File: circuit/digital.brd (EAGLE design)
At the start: 56.2 x 50.8 mm, 31 parts, among them IC1 MCP1701-5V, IC2 MCP1700-3.3V, X1 MINI-USB-SCHIELD-32005-301

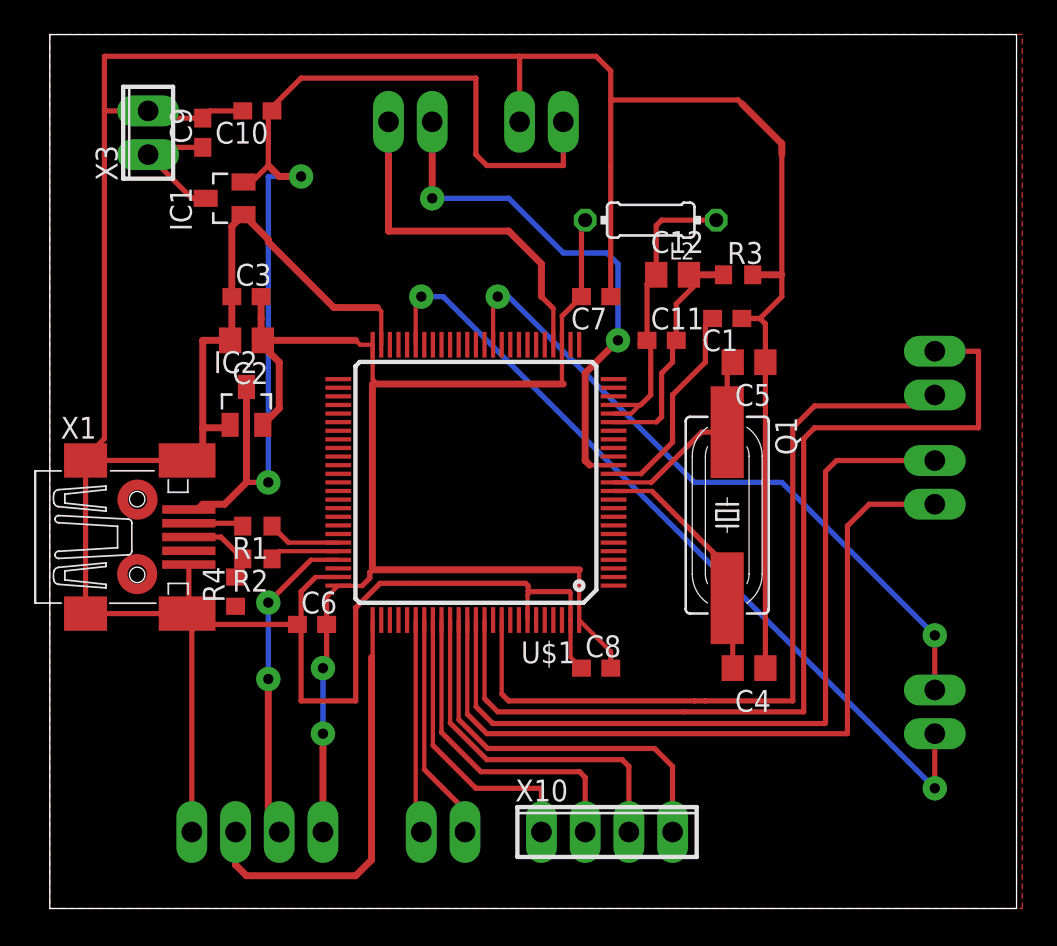
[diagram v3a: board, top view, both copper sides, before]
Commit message: - на цифровой схеме добавили разъем для Nokia 5110, коннекторы для переключения питания, объединили восточный разъем - на аналоговой схеме добавили включение 3.3 nF конденсатор, для фильтрации высокочастотных шумов ADC
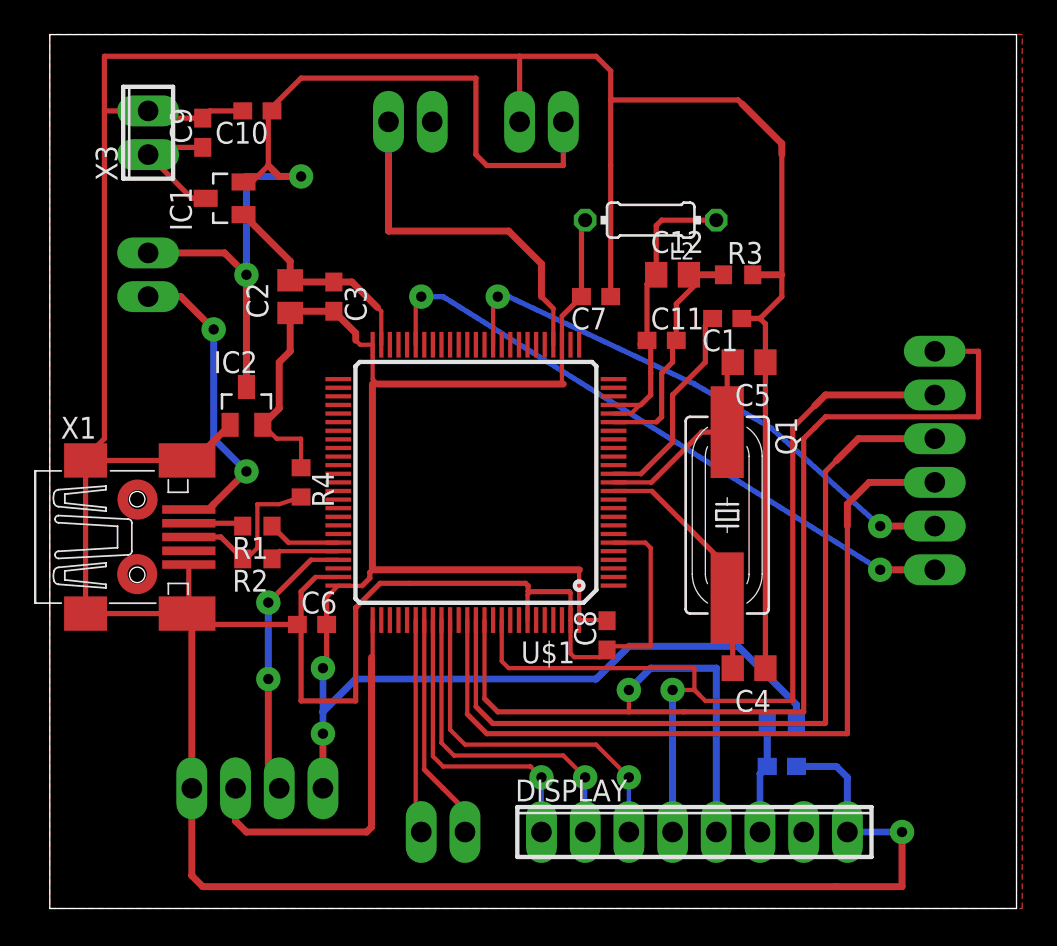
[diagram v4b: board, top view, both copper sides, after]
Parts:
- removed X10: (no value), con-phoenix-254:4POL254
- removed X6, X7: (no value), con-phoenix-254:2POL254
- added C13: 1mk, rcl:C0603
- added DISPLAY: (no value), con-phoenix-254:8POL254
- added R5: 22, rcl:R0603
- added X11: (no value), con-phoenix-254:6POL254
- moved X5 52.3 mm to (5.71, 36.8), turned to 90 degrees
- moved R4 7.41 mm to (14.6, 24.8), turned to 270 degrees
- moved C3 5.08 mm to (16.5, 35.6), turned to 270 degrees
- moved C2 3.59 mm to (14.0, 35.6), turned to 90 degrees
- moved X9 2.54 mm to (12.1, 6.99)
- moved C8 2.01 mm to (32.4, 15.9), turned to 90 degrees
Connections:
- removed net ADC12_IN6: U$1.15, X8.2
- removed net N$10: U$1.86, X10.4
- removed net N$9: U$1.85, X10.3
- new net D_CE: DISPLAY.2, U$1.84
- new net D_DC: DISPLAY.3, U$1.85
- new net D_RST: DISPLAY.1, U$1.83
- new net N$13: DISPLAY.7
- net +3V3: now also R5.1
- net +5V: now also X5.2; no longer X1.1
- net GND: now also C13.1, DISPLAY.8
- net I_ADC: now also X11.6; no longer X5.2
- net N$6: now also C13.2, DISPLAY.6, R5.2; no longer U$1.83, X10.1
- net N$8: now also X1.1, X5.1; no longer U$1.84, X10.2
- net SPI1_MOSI: now also DISPLAY.4, X11.2; no longer X6.2
- net SPI1_SCK: now also DISPLAY.5, X11.1; no longer X6.1
- net SPI_CS_I: now also X11.4; no longer X7.2
- net SPI_CS_V: now also X11.3; no longer X7.1
- net V_ADC: now also X11.5; no longer X5.1
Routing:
- net GND: track 235.6 -> 290.0 mm, vias 0 -> 1
- net ADC12_IN6: track 30.8 -> 0.00 mm, vias 2 -> 0
- net +3V3: track 85.0 -> 114.6 mm
- net N$10: track 23.2 -> 0.00 mm
- net N$9: track 21.2 -> 0.00 mm
- net D_DC: track 0.00 -> 21.1 mm, vias 0 -> 1
- net D_CE: track 0.00 -> 19.5 mm, vias 0 -> 1
- net D_RST: track 0.00 -> 17.9 mm, vias 0 -> 1
- net SPI1_SCK: track 56.7 -> 72.7 mm, vias 0 -> 1
- net N$6: track 17.2 -> 6.52 mm
- net I_ADC: track 48.2 -> 37.8 mm
- net SPI1_MOSI: track 46.4 -> 55.9 mm, vias 0 -> 1
- net +5V: track 62.9 -> 54.0 mm
- net V_ADC: track 40.0 -> 32.7 mm
- net N$2: track 3.66 -> 9.92 mm
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
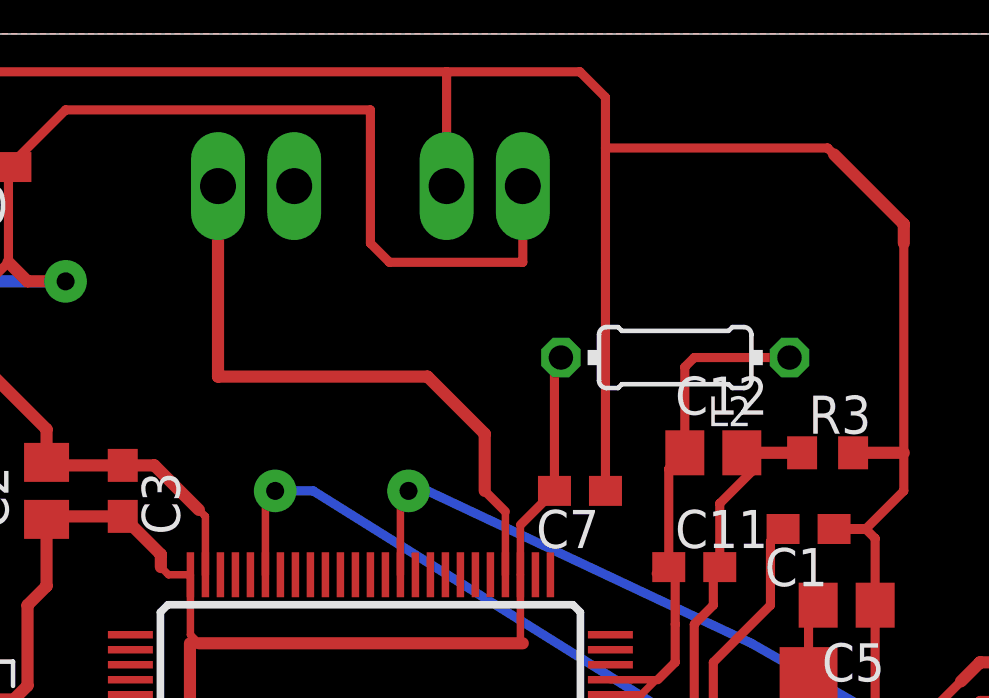
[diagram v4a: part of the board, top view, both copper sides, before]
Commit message: - перенесли конденсаторы фильтрующие частоту для ADC на цифровую часть схемы
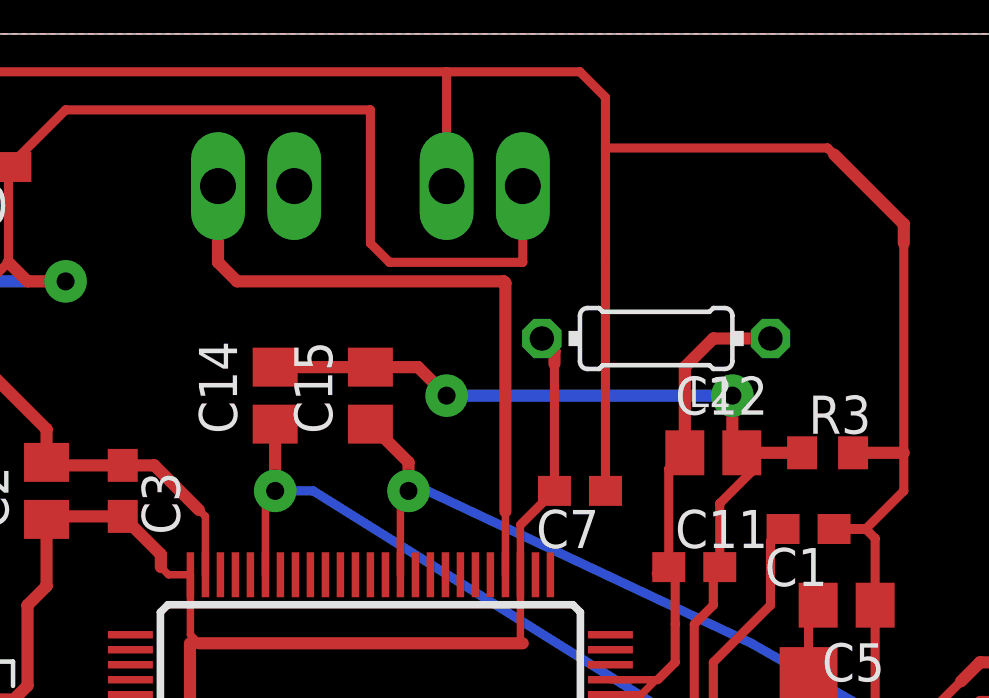
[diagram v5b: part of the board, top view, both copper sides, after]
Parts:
- added C14, C15: 330pF, rcl:C0805
- moved L2 0.90 mm to (34.3, 40.6)
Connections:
- net GNDA: now also C14.2, C15.2
- net I_ADC: now also C14.1
- net V_ADC: now also C15.1
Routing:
- net GNDA: track 14.1 -> 31.8 mm, vias 0 -> 2
- net V_ADC: track 32.7 -> 35.4 mm
- net I_ADC: track 37.8 -> 40.0 mm
- net GENERATOR: track 21.0 -> 22.1 mm
- net +3V3: track 114.6 -> 115.3 mm
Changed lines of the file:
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@@
 </autorouter>
 <elements>
-<element name="L2" library="rcl" package="0204/7" value="100mk" x="34.925" y="40.005" rot="R180"/>
+<element name="L2" library="rcl" package="0204/7" value="100mk" x="34.29" y="40.64" rot="R180"/>
 <element name="C11" library="rcl" package="C0603" value="100n" x="35.56" y="33.02"/>
 <element name="C12" library="rcl" package="C0805" value="10mk" x="36.195" y="36.83"/>
@@
 <attribute name="OC_FARNELL" value="unknown" x="5.715" y="36.83" size="1.778" layer="28" rot="MR90" display="off"/>
 </element>
+<element name="C14" library="rcl" package="C0805" value="330pF" x="21.59" y="38.735" rot="R90"/>
+<element name="C15" library="rcl" package="C0805" value="330pF" x="24.765" y="38.735" rot="R90"/>
 </elements>
 <signals>
@@
 <contactref element="X8" pad="1"/>
 <contactref element="U$1" pad="29"/>
-<wire x1="29.265" y1="34.87" x2="28.575" y2="35.56" width="0.3048" layer="1"/>
-<wire x1="28.575" y1="35.56" x2="28.575" y2="37.465" width="0.4064" layer="1"/>
-<wire x1="28.575" y1="37.465" x2="26.67" y2="39.37" width="0.4064" layer="1"/>
-<wire x1="26.67" y1="39.37" x2="19.685" y2="39.37" width="0.4064" layer="1"/>
-<wire x1="19.685" y1="39.37" x2="19.685" y2="45.72" width="0.4064" layer="1"/>
 <wire x1="29.265" y1="32.765" x2="29.265" y2="34.87" width="0.25" layer="1"/>
+<wire x1="29.265" y1="34.87" x2="29.265" y2="42.49" width="0.4064" layer="1"/>
+<wire x1="29.265" y1="42.49" x2="29.21" y2="42.545" width="0.4064" layer="1"/>
+<wire x1="29.21" y1="42.545" x2="20.32" y2="42.545" width="0.4064" layer="1"/>
+<wire x1="20.32" y1="42.545" x2="19.685" y2="43.18" width="0.4064" layer="1"/>
+<wire x1="19.685" y1="43.18" x2="19.685" y2="45.72" width="0.4064" layer="1"/>
 </signal>
 <signal name="+5V">
@@
 <wire x1="32.765" y1="28.265" x2="35.25" y2="28.265" width="0.25" layer="1"/>
 <wire x1="37.145" y1="36.83" x2="39.155" y2="36.83" width="0.4064" layer="1"/>
+<contactref element="C14" pad="2"/>
+<contactref element="C15" pad="2"/>
+<wire x1="24.765" y1="39.685" x2="26.355" y2="39.685" width="0.4064" layer="1"/>
+<wire x1="26.355" y1="39.685" x2="27.305" y2="38.735" width="0.4064" layer="1"/>
+<via x="27.305" y="38.735" extent="1-16" drill="0.6" diameter="1.4224" shape="square"/>
+<wire x1="27.305" y1="38.735" x2="36.83" y2="38.735" width="0.4064" layer="16"/>
+<via x="36.83" y="38.735" extent="1-16" drill="0.6" diameter="1.4224" shape="square"/>
+<wire x1="36.83" y1="38.735" x2="36.83" y2="37.145" width="0.4064" layer="1"/>
+<wire x1="36.83" y1="37.145" x2="37.145" y2="36.83" width="0.4064" layer="1"/>
+<wire x1="21.59" y1="39.685" x2="24.765" y2="39.685" width="0.4064" layer="1"/>
 </signal>
 <signal name="V_ADC">
@@
 <contactref element="X11" pad="5"/>
 <wire x1="48.26" y1="22.225" x2="51.435" y2="22.225" width="0.4064" layer="1"/>
+<contactref element="C15" pad="1"/>
+<wire x1="26.035" y1="35.56" x2="26.035" y2="36.515" width="0.4064" layer="1"/>
+<wire x1="26.035" y1="36.515" x2="24.765" y2="37.785" width="0.4064" layer="1"/>
 </signal>
 <signal name="RA">
@@
 <contactref element="X11" pad="6"/>
 <wire x1="48.26" y1="19.685" x2="51.435" y2="19.685" width="0.4064" layer="1"/>
+<contactref element="C14" pad="1"/>
+<wire x1="21.59" y1="37.785" x2="21.59" y2="35.56" width="0.4064" layer="1"/>
 </signal>
 <signal name="SPI_CS_V">
@@
 <wire x1="19.05" y1="30.48" x2="18.75" y2="30.48" width="0.3048" layer="1"/>
 <wire x1="30.9" y1="35.56" x2="30.9" y2="39.79" width="0.3048" layer="1"/>
-<wire x1="30.9" y1="39.79" x2="31.115" y2="40.005" width="0.3048" layer="1"/>
 <contactref element="X9" pad="1"/>
 <wire x1="16.09" y1="16.51" x2="16.09" y2="14.185" width="0.3048" layer="1"/>
@@
 <wire x1="13.97" y1="34.61" x2="13.97" y2="32.385" width="0.4064" layer="1"/>
 <wire x1="13.97" y1="32.385" x2="13.335" y2="31.75" width="0.4064" layer="1"/>
+<wire x1="30.9" y1="39.79" x2="30.9" y2="40.22" width="0.4064" layer="1"/>
+<wire x1="30.9" y1="40.22" x2="30.48" y2="40.64" width="0.4064" layer="1"/>
 </signal>
 <signal name="V+">
@@
 <wire x1="34.71" y1="33.02" x2="34.71" y2="36.295" width="0.3048" layer="1"/>
 <wire x1="34.71" y1="36.295" x2="35.245" y2="36.83" width="0.3048" layer="1"/>
-<wire x1="35.245" y1="36.83" x2="35.245" y2="39.69" width="0.3048" layer="1"/>
-<wire x1="35.245" y1="39.69" x2="35.56" y2="40.005" width="0.3048" layer="1"/>
-<wire x1="35.56" y1="40.005" x2="38.735" y2="40.005" width="0.3048" layer="1"/>
 <wire x1="32.765" y1="29.265" x2="34.29" y2="29.265" width="0.25" layer="1"/>
 <wire x1="34.29" y1="29.265" x2="34.345" y2="29.265" width="0.25" layer="1"/>
 <wire x1="32.765" y1="28.765" x2="33.79" y2="28.765" width="0.25" layer="1"/>
 <wire x1="33.79" y1="28.765" x2="34.29" y2="29.265" width="0.25" layer="1"/>
+<wire x1="38.1" y1="40.64" x2="36.195" y2="40.64" width="0.4064" layer="1"/>
+<wire x1="36.195" y1="40.64" x2="35.245" y2="39.69" width="0.4064" layer="1"/>
+<wire x1="35.245" y1="36.83" x2="35.245" y2="39.69" width="0.4064" layer="1"/>
 </signal>
 <signal name="N$4">

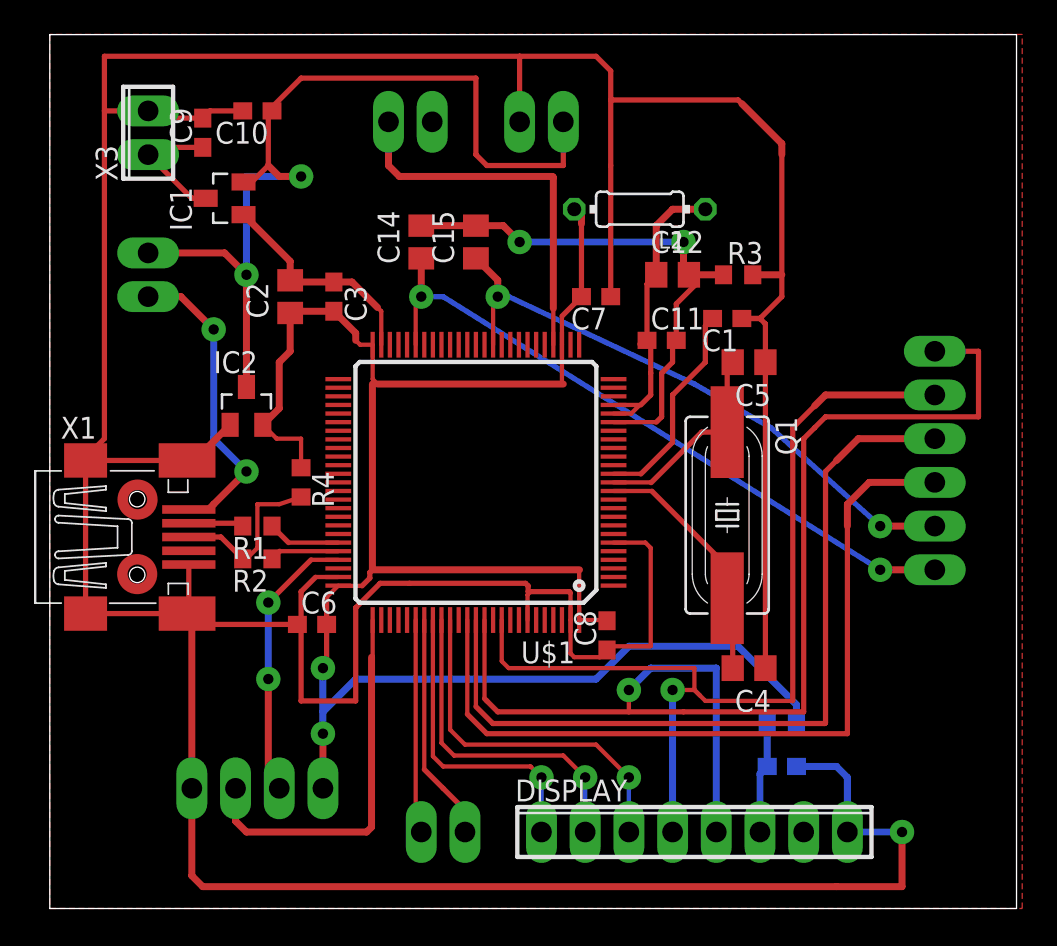
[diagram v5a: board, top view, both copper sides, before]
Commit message: - совместили северные контакты - добавили RC цепочки между первым и вторым каскадом усиления - добавили неподключеный коннектор, чтобы было на чем держаться дисплею
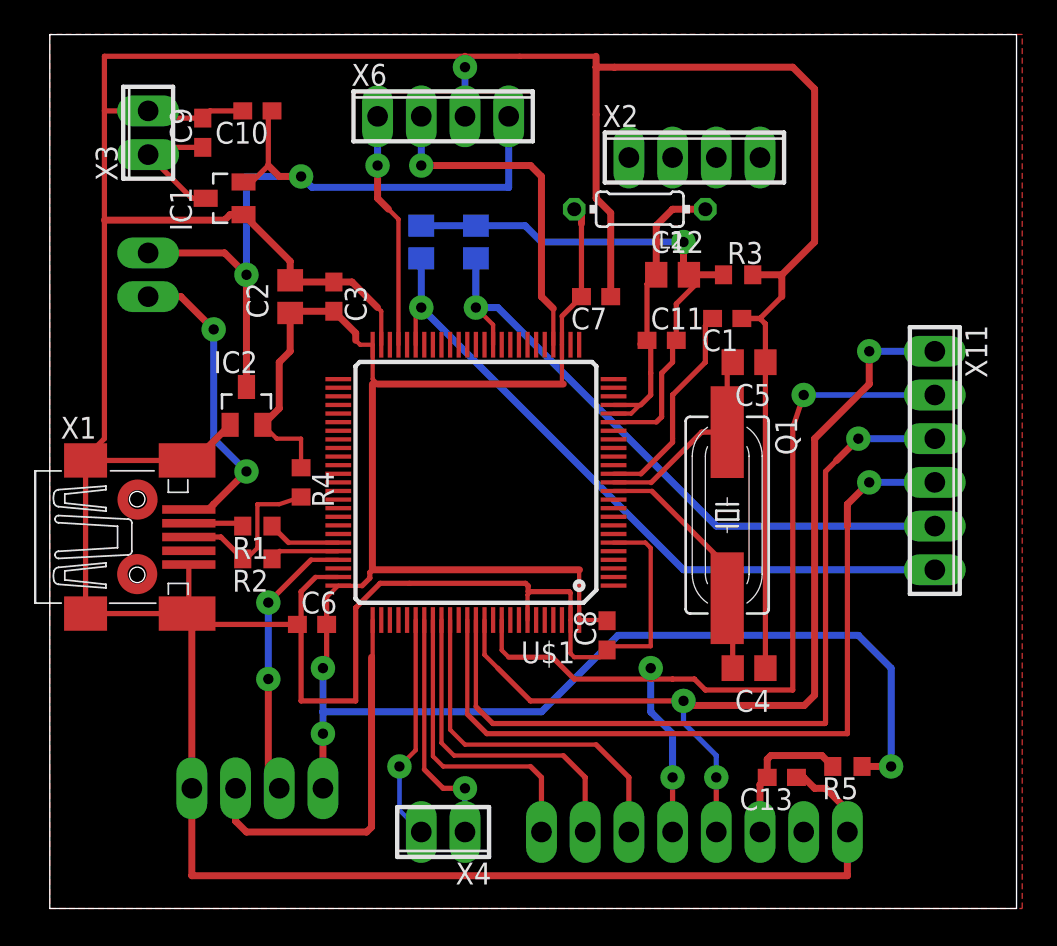
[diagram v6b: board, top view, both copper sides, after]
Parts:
- removed X8: (no value), con-phoenix-254:2POL254
- added X6: (no value), con-phoenix-254:4POL254
- X2: device con-phoenix-254:2POL254 -> con-phoenix-254:4POL254
- moved X2 9.13 mm to (37.5, 43.6), flipped to the top
- moved R5 4.58 mm to (46.4, 8.26), flipped to the top, turned to 180 degrees
- moved C13 0.64 mm to (42.5, 7.62), flipped to the top, turned to 180 degrees
- flipped C14 to the bottom
- flipped C15 to the bottom
- flipped DISPLAY to the bottom, turned to 180 degrees
- flipped X11 to the top
- flipped X4 to the top, turned to 180 degrees
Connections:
- new net AN_SW: U$1.47, X6.1
- net +5V: now also X6.4; no longer X2.1
- net GENERATOR: now also X6.2; no longer X8.1
- net GND: now also X6.3; no longer X2.2
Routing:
- net SPI1_SCK: track 72.7 -> 56.2 mm, vias 1 -> 3
- net AN_SW: track 0.00 -> 13.8 mm, vias 0 -> 1
- net +3V3: track 115.3 -> 126.8 mm, vias 2 -> 3
- net +5V: track 54.0 -> 45.6 mm
- net GND: track 290.0 -> 295.5 mm
- net N$6: track 6.52 -> 8.57 mm
- net GENERATOR: track 22.1 -> 20.2 mm, vias 0 -> 1
- net V_ADC: track 35.4 -> 37.4 mm, vias 2 -> 1
- net I_ADC: track 40.0 -> 41.3 mm, vias 2 -> 1
- net RA: track 13.3 -> 14.0 mm, vias 0 -> 1
- net SPI1_MOSI: track 55.9 -> 55.2 mm, vias 1 -> 3
- net RB: track 12.9 -> 13.2 mm, vias 0 -> 1
- net GNDA: vias 2 -> 1
- net D_CE: vias 1 -> 0
- net SPI_CS_V: vias 0 -> 1
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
